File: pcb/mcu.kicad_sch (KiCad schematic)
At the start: 15 parts, among them J1 AVR-UPDI-6, U1 ATtiny1616-MNR

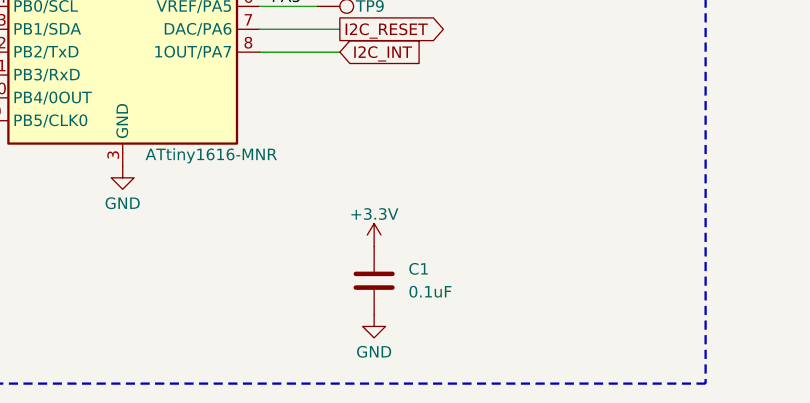
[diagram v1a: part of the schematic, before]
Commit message: Redesign with cutouts for sensors
Removed power connectors since 5V is not needed
Added cutout for VOC sensor
Rerouted sensor section
Rescaled logos and fixed silkscreen
Changed to blue LED for power indicator
Updated requirements and renders
Changed all 0.1uF caps to small symbol
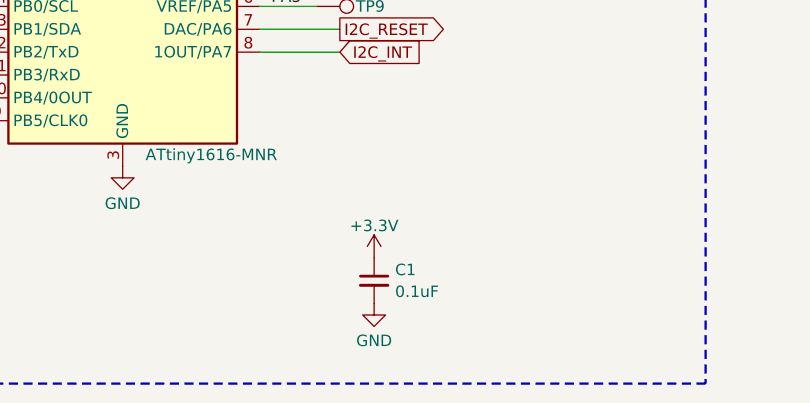
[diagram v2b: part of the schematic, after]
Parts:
- C1: symbol Device:C -> Device:C_Small
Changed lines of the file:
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@@
 	(symbol
 		(lib_id "power:GND")
-		(at 113.03 91.44 0)
+		(at 113.03 90.17 0)
 		(unit 1)
 		(exclude_from_sim no)
@@
 		(fields_autoplaced yes)
 		(property "Reference" "#PWR06"
-			(at 113.03 97.79 0)
+			(at 113.03 96.52 0)
 			(effects
 				(font
@@
 		)
 		(property "Value" "GND"
-			(at 113.03 95.5731 0)
+			(at 113.03 94.3031 0)
 			(effects
 				(font
@@
 		)
 		(property "Footprint" ""
-			(at 113.03 91.44 0)
+			(at 113.03 90.17 0)
 			(effects
 				(font
@@
 		)
 		(property "Datasheet" ""
-			(at 113.03 91.44 0)
+			(at 113.03 90.17 0)
 			(effects
 				(font
@@
 		)
 		(property "Description" "Power symbol creates a global label with name \"GND\" , ground"
-			(at 113.03 91.44 0)
+			(at 113.03 90.17 0)
 			(effects
 				(font
@@
 	)
 	(symbol
-		(lib_id "Device:C")
+		(lib_id "Device:C_Small")
 		(at 113.03 87.63 0)
 		(unit 1)
@@
 		(fields_autoplaced yes)
 		(property "Reference" "C1"
-			(at 116.84 86.3599 0)
+			(at 115.3541 86.4241 0)
 			(effects
 				(font
@@
 		)
 		(property "Value" "0.1uF"
-			(at 116.84 88.8999 0)
+			(at 115.3541 88.8484 0)
 			(effects
 				(font
@@
 		)
 		(property "Footprint" "CRGM Passive:C_0603_1608Metric"
-			(at 113.9952 91.44 0)
+			(at 113.03 87.63 0)
 			(effects
 				(font
@@
 			)
 		)
-		(property "Description" "Unpolarized capacitor"
+		(property "Description" "Unpolarized capacitor, small symbol"
 			(at 113.03 87.63 0)
 			(effects
@@
 	(symbol
 		(lib_id "power:+3.3V")
-		(at 113.03 83.82 0)
+		(at 113.03 85.09 0)
 		(unit 1)
 		(exclude_from_sim no)
@@
 		(dnp no)
 		(property "Reference" "#PWR05"
-			(at 113.03 87.63 0)
+			(at 113.03 88.9 0)
 			(effects
 				(font
@@
 		)
 		(property "Value" "+3.3V"
-			(at 113.03 80.264 0)
+			(at 113.03 81.534 0)
 			(effects
 				(font
@@
 		)
 		(property "Footprint" ""
-			(at 113.03 83.82 0)
+			(at 113.03 85.09 0)
 			(effects
 				(font
@@
 		)
 		(property "Datasheet" ""
-			(at 113.03 83.82 0)
+			(at 113.03 85.09 0)
 			(effects
 				(font
@@
 		)
 		(property "Description" "Power symbol creates a global label with name \"+3.3V\""
-			(at 113.03 83.82 0)
-			(effects
-				(font
+			(at 113.03 85.09 0)
+			(effects
+				(font

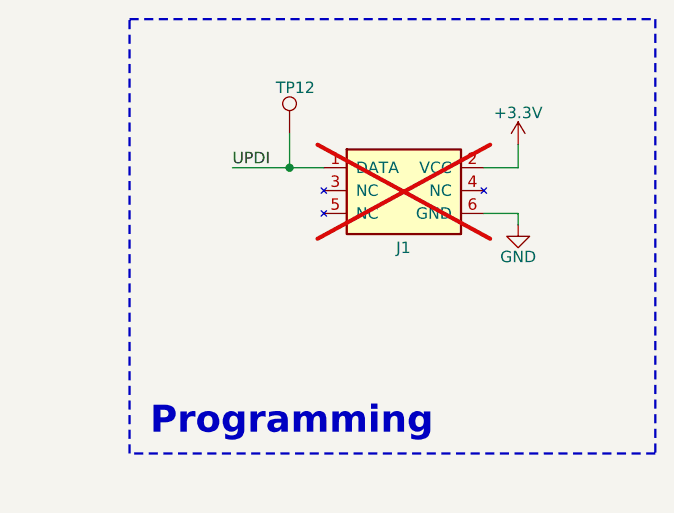
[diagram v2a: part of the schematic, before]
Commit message: Updated UPDI Connector
Integrated serial and UPDI
Changed to vertical connectors
Updated renders
Rounded cutouts
Adjusted silkscreen
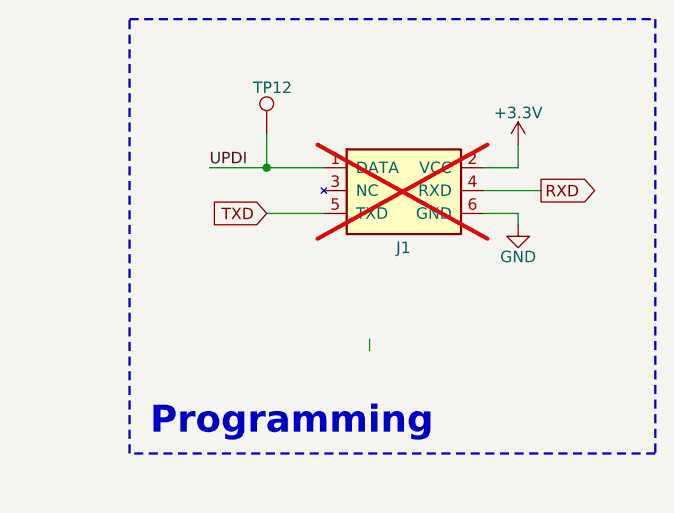
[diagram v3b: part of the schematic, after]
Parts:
- J1: symbol CRGM Connector:AVR-UPDI-6 -> CRGM Connector:AVR-UPDI-UART-6
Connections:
- net RXD: now also J1.4 (RXD)
- net TXD: now also J1.5 (TXD)
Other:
- moved on the sheet: TP12
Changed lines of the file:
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@@
 	)
 	(junction
-		(at 195.58 41.91)
+		(at 193.04 41.91)
 		(diameter 0)
 		(color 0 0 0 0)
@@
 	(wire
 		(pts
-			(xy 195.58 41.91) (xy 199.39 41.91)
+			(xy 217.17 44.45) (xy 223.52 44.45)
+		)
+		(stroke
+			(width 0)
+			(type default)
+		)
+	)
+	(wire
+		(pts
+			(xy 193.04 41.91) (xy 199.39 41.91)
 		)
 		(stroke
@@
 	(wire
 		(pts
-			(xy 189.23 41.91) (xy 195.58 41.91)
+			(xy 186.69 41.91) (xy 193.04 41.91)
+		)
+		(stroke
+			(width 0)
+			(type default)
+		)
+	)
+	(wire
+		(pts
+			(xy 204.47 62.23) (xy 204.47 60.96)
 		)
 		(stroke
@@
 	(wire
 		(pts
-			(xy 195.58 38.1) (xy 195.58 41.91)
+			(xy 193.04 38.1) (xy 193.04 41.91)
 		)
 		(stroke
@@
 		(pts
 			(xy 85.09 35.56) (xy 85.09 39.37)
+		)
+		(stroke
+			(width 0)
+			(type default)
+		)
+	)
+	(wire
+		(pts
+			(xy 193.04 46.99) (xy 199.39 46.99)
 		)
 		(stroke
@@
 	)
 	(label "UPDI"
-		(at 189.23 41.91 0)
+		(at 186.69 41.91 0)
 		(effects
 			(font
@@
 		)
 	)
+	(global_label "RXD"
+		(shape output)
+		(at 223.52 44.45 0)
+		(fields_autoplaced yes)
+		(effects
+			(font
+				(size 1.27 1.27)
+			)
+			(justify left)
+		)
+		(property "Intersheetrefs" "${INTERSHEET_REFS}"
+			(at 230.2547 44.45 0)
+			(effects
+				(font
+					(size 1.27 1.27)
+				)
+				(justify left)
+			)
+		)
+	)
 	(global_label "MCU_SCL"
 		(shape output)
@@
 				)
 				(justify left)
+			)
+		)
+	)
+	(global_label "TXD"
+		(shape input)
+		(at 193.04 46.99 180)
+		(fields_autoplaced yes)
+		(effects
+			(font
+				(size 1.27 1.27)
+			)
+			(justify right)
+		)
+		(property "Intersheetrefs" "${INTERSHEET_REFS}"
+			(at 186.6077 46.99 0)
+			(effects
+				(font
+					(size 1.27 1.27)
+				)
+				(justify right)
 			)
 		)
@@
 	)
 	(symbol
-		(lib_id "CRGM Connector:AVR-UPDI-6")
+		(lib_id "CRGM Connector:AVR-UPDI-UART-6")
 		(at 208.28 45.72 0)
 		(unit 1)
@@
 		)
 		(property "Footprint" "CRGM Connector:PinHeader_2x03_P2.54mm_Vertical_SMD"
-			(at 201.93 46.99 90)
+			(at 208.28 58.674 0)
 			(effects
 				(font
@@
 			)
 		)
-		(property "Description" "Atmel 6-pin UPDI connector"
+		(property "Description" "Atmel 6-pin UPDI + UART connector"
 			(at 208.28 56.388 0)
 			(effects
@@
 	(symbol
 		(lib_id "CRGM Connector:TestPoint")
-		(at 195.58 38.1 0)
+		(at 193.04 38.1 0)
 		(unit 1)
 		(exclude_from_sim no)
@@
 		(dnp no)
 		(property "Reference" "TP12"
-			(at 194.056 33.02 0)
+			(at 191.516 33.02 0)
 			(effects
 				(font
@@
 		)
 		(property "Value" "~"
-			(at 193.294 33.0199 0)
+			(at 190.754 33.0199 0)
 			(effects
 				(font
@@
 		)
 		(property "Footprint" "CRGM Mechanical:TestPoint_Pad_D1.0mm"
-			(at 195.58 45.466 0)
+			(at 193.04 45.466 0)
 			(effects
 				(font
@@
 		)
 		(property "Datasheet" "~"
-			(at 197.866 36.068 0)
+			(at 195.326 36.068 0)
 			(effects
 				(font
@@
 		)
 		(property "Description" "Test Point D1.0mm"
-			(at 195.58 47.244 0)
+			(at 193.04 47.244 0)
 			(effects
 				(font
@@
 		)
 		(property "LCSC" ""
-			(at 195.58 38.1 0)
+			(at 193.04 38.1 0)
 			(effects
 				(font
@@
 		)
 		(property "Digikey" ""
-			(at 195.58 38.1 0)
+			(at 193.04 38.1 0)
 			(effects
 				(font
@@
 		)
 		(property "Mouser" ""
-			(at 195.58 38.1 0)
-			(effects
-				(font
+			(at 193.04 38.1 0)
+			(effects
+				(font

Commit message: Closed #3
Added status LEDs -- updated
Updated renders
Updated silkscreen
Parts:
- removed TP1, TP2, TP3: ~, CRGM Mechanical:TestPoint_Pad_D1.0mm, symbol CRGM Connector:TestPoint
- added D3, D4, D9: Blue, CRGM Passive:LED_0603_1608Metric, symbol Device:LED_Small
- added R15, R20, R22: 1K, CRGM Passive:R_0603_1608Metric, symbol Device:R_Small
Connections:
- net +3.3V: now also R15.1, R20.1, R22.1
- net PC0 renamed LED_VOC
- net LED_VOC: now also D9.1 (K)
- net PC1 renamed LED_LIGHT
- net LED_LIGHT: now also D4.1 (K)
- net PC2 renamed LED_TEMP
- net LED_TEMP: now also D3.1 (K)
- new net: D4.2 (A), R22.2
- new net: D3.2 (A), R15.2
- new net: D9.2 (A), R20.2
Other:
- note added: "Indicator"
- moved on the sheet: C1, J1, JP1, JP2, TP12, TP4, TP5, TP6, TP7, TP8, TP9, U1

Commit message: Adjusted spacing and alignment of parts
Moved temp and voc to be on grid
Updated renders
Ran ERC -- fixed errors
Ran DRC -- fixed errors
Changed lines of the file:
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@@
-	(wire
-		(pts
-			(xy 204.47 62.23) (xy 204.47 60.96)
-		)
-		(stroke
-			(width 0)
-			(type default)
-		)
-	)
 	(wire
 		(pts
